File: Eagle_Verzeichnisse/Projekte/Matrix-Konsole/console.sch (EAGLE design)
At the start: 15 parts, among them J1 DIN5, J2 DIN5, J3 DIN5, J4 DIN5, X2 057-016-1

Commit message: Added Spannungsregler
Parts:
- removed D1: 5V, diode:ZENER-DIODEDO35Z10
- removed R3: 10, resistor:R-EU_M3516
- added U$1: SPGRGL_DEV, Spannungsregler:SPGRGL_DEV
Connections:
- removed net N$3: D1.C, JP2.1, JP2.2, R3.1
- new net N$1: JP2.1, JP2.2, U$1.OUT+
- new net N$8: JP2.3, JP2.4, U$1.OUT-
- net GND: now also U$1.IN-; no longer D1.A, JP2.3, JP2.4
- net VCC: now also U$1.IN+; no longer R3.2

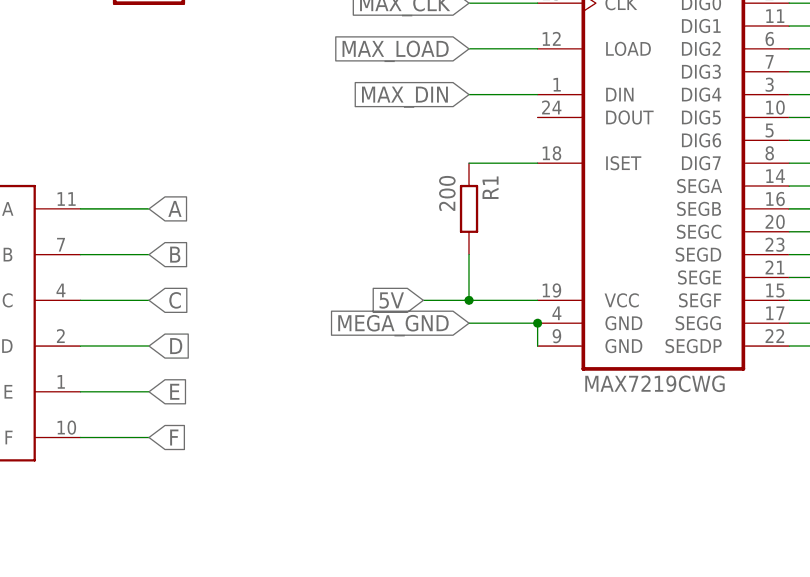
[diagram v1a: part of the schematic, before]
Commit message: Added Layout for console
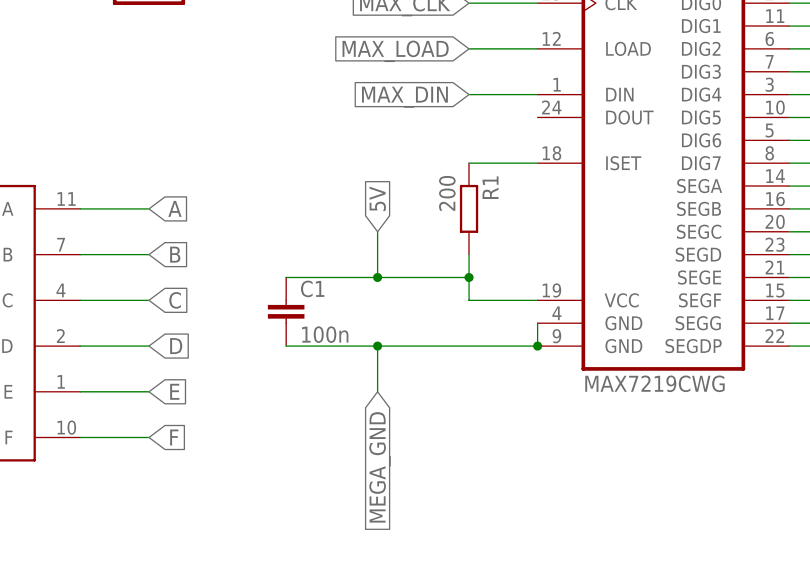
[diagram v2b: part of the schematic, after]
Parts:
- added C1: 100n, eagle-ltspice:C
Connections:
- net 5V: now also C1.1
- net MEGA_GND: now also C1.2
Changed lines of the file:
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@@
 <setting verticaltext="up"/>
 </settings>
-<grid distance="0.1" unitdist="inch" unit="inch" style="lines" multiple="1" display="yes" altdistance="0.01" altunitdist="inch" altunit="inch"/>
+<grid distance="0.1" unitdist="inch" unit="inch" style="lines" multiple="1" display="no" altdistance="0.01" altunitdist="inch" altunit="inch"/>
 <layers>
 <layer number="1" name="Top" color="4" fill="1" visible="no" active="no"/>
@@
 <part name="JP2" library="pinhead" deviceset="PINHD-1X4" device=""/>
 <part name="JP1" library="pinhead" deviceset="PINHD-1X25" device=""/>
+<part name="GND1" library="supply1" deviceset="GND" device=""/>
+<part name="C1" library="eagle-ltspice" deviceset="C" device="" value="100n"/>
 <part name="U$1" library="Spannungsregler" deviceset="SPGRGL_DEV" device=""/>
-<part name="GND1" library="supply1" deviceset="GND" device=""/>
 </parts>
 <sheets>
@@
 <instance part="JP2" gate="A" x="175.26" y="25.4"/>
 <instance part="JP1" gate="A" x="55.88" y="99.06"/>
+<instance part="GND1" gate="1" x="124.46" y="20.32"/>
+<instance part="C1" gate="G$1" x="187.96" y="-12.7"/>
 <instance part="U$1" gate="G$1" x="144.78" y="27.94"/>
-<instance part="GND1" gate="1" x="124.46" y="20.32"/>
 </instances>
 <busses>
@@
 </segment>
 <segment>
-<pinref part="U$1" gate="G$1" pin="IN+"/>
 <wire x1="134.28" y1="31.44" x2="124.46" y2="31.44" width="0.1524" layer="91"/>
 <label x="124.206" y="31.496" size="1.778" layer="95" rot="R180" xref="yes"/>
+<pinref part="U$1" gate="G$1" pin="IN+"/>
 </segment>
 </net>
@@
 </segment>
 <segment>
-<pinref part="U$1" gate="G$1" pin="IN-"/>
 <wire x1="134.28" y1="24.94" x2="124.46" y2="24.94" width="0.1524" layer="91"/>
 <wire x1="124.46" y1="24.94" x2="124.46" y2="22.86" width="0.1524" layer="91"/>
 <pinref part="GND1" gate="1" pin="GND"/>
+<pinref part="U$1" gate="G$1" pin="IN-"/>
 </segment>
 </net>
@@
 <segment>
 <wire x1="215.9" y1="-12.7" x2="208.28" y2="-12.7" width="0.1524" layer="91"/>
-<wire x1="208.28" y1="-7.62" x2="208.28" y2="-12.7" width="0.1524" layer="91"/>
-<wire x1="208.28" y1="-12.7" x2="203.2" y2="-12.7" width="0.1524" layer="91"/>
-<junction x="208.28" y="-12.7"/>
-<label x="203.2" y="-12.7" size="1.778" layer="95" rot="R180" xref="yes"/>
+<wire x1="208.28" y1="-7.62" x2="208.28" y2="-10.16" width="0.1524" layer="91"/>
 <pinref part="U$2" gate="G$1" pin="VCC"/>
 <pinref part="R1" gate="G$1" pin="2"/>
+<pinref part="C1" gate="G$1" pin="1"/>
+<wire x1="208.28" y1="-10.16" x2="208.28" y2="-12.7" width="0.1524" layer="91"/>
+<wire x1="208.28" y1="-10.16" x2="198.12" y2="-10.16" width="0.1524" layer="91"/>
+<junction x="208.28" y="-10.16"/>
+<wire x1="198.12" y1="-10.16" x2="187.96" y2="-10.16" width="0.1524" layer="91"/>
+<wire x1="198.12" y1="-10.16" x2="198.12" y2="-5.08" width="0.1524" layer="91"/>
+<junction x="198.12" y="-10.16"/>
+<label x="198.12" y="-5.08" size="1.778" layer="95" rot="R90" xref="yes"/>
 </segment>
 <segment>
@@
 <segment>
 <wire x1="215.9" y1="-15.24" x2="215.9" y2="-17.78" width="0.1524" layer="91"/>
-<wire x1="215.9" y1="-15.24" x2="208.28" y2="-15.24" width="0.1524" layer="91"/>
 <pinref part="U$2" gate="G$1" pin="GND@2"/>
 <pinref part="U$2" gate="G$1" pin="GND@1"/>
-<junction x="215.9" y="-15.24"/>
-<label x="208.28" y="-15.24" size="1.778" layer="95" rot="R180" xref="yes"/>
+<pinref part="C1" gate="G$1" pin="2"/>
+<wire x1="187.96" y1="-17.78" x2="198.12" y2="-17.78" width="0.1524" layer="91"/>
+<junction x="215.9" y="-17.78"/>
+<wire x1="198.12" y1="-17.78" x2="215.9" y2="-17.78" width="0.1524" layer="91"/>
+<wire x1="198.12" y1="-17.78" x2="198.12" y2="-22.86" width="0.1524" layer="91"/>
+<junction x="198.12" y="-17.78"/>
+<label x="198.12" y="-22.86" size="1.778" layer="95" rot="R270" xref="yes"/>
 </segment>
 <segment>
@@
 <pinref part="JP2" gate="A" pin="4"/>
 <wire x1="172.72" y1="22.86" x2="167.64" y2="22.86" width="0.1524" layer="91"/>
-<pinref part="U$1" gate="G$1" pin="OUT-"/>
 <wire x1="154.78" y1="24.94" x2="167.64" y2="24.94" width="0.1524" layer="91"/>
 <wire x1="167.64" y1="24.94" x2="167.64" y2="25.4" width="0.1524" layer="91"/>
+<pinref part="U$1" gate="G$1" pin="OUT-"/>
 </segment>
 </net>
@@
 <wire x1="172.72" y1="27.94" x2="167.64" y2="27.94" width="0.1524" layer="91"/>
 <wire x1="167.64" y1="27.94" x2="167.64" y2="30.48" width="0.1524" layer="91"/>
-<pinref part="U$1" gate="G$1" pin="OUT+"/>
 <wire x1="154.78" y1="31.44" x2="167.64" y2="31.44" width="0.1524" layer="91"/>
 <wire x1="167.64" y1="31.44" x2="167.64" y2="30.48" width="0.1524" layer="91"/>
 <junction x="167.64" y="30.48"/>
-</segment>
-</net>
+<pinref part="U$1" gate="G$1" pin="OUT+"/>
+</segment>
+</net>
